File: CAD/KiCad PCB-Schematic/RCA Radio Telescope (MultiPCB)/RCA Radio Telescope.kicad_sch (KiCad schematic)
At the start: 10 parts, among them J1 Screw_Terminal_01x04, J12 3V In For LNA, J2 9-12V From PoE Splitter, J3 3V Out For LNA, J4 5V Out For Filter Board, J6 USB_B_MICRO, U1 ZX60-P33ULN+, U2 ADALM Pluto SDR

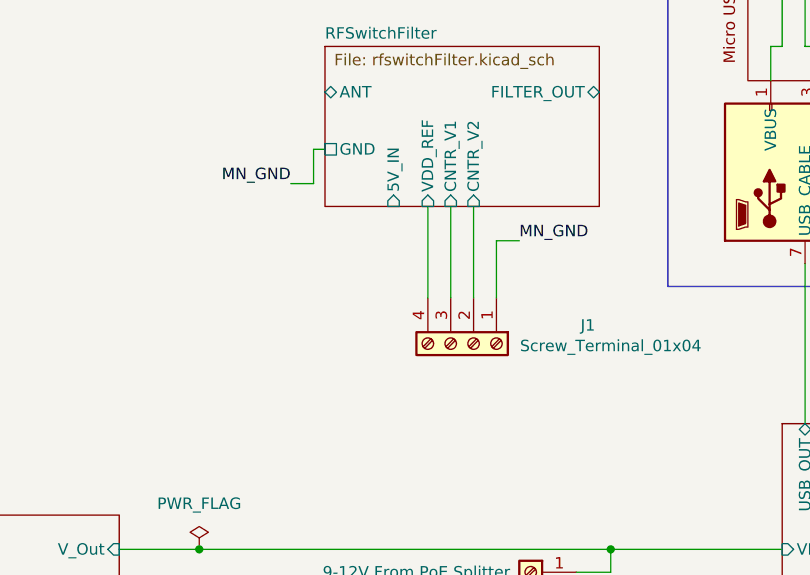
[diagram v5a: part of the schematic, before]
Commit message: Added 4 RF Board Designs into KiCAD project
- Added Matched SMD Filter Board, Matched Distributive Filter Board, RF Switch Filter Board, and kept original SMD Filter Board
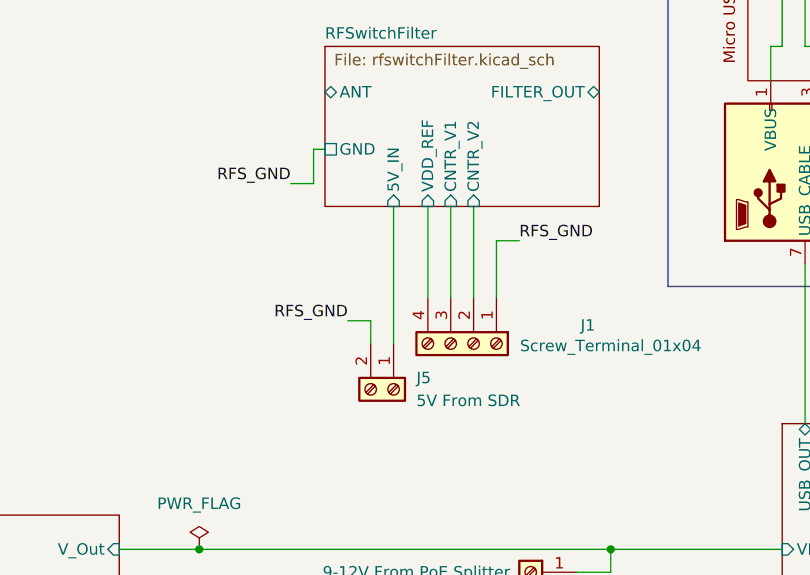
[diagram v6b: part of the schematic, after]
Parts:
- added J5: 5V From SDR, Library:CONN_1729128_PXC, symbol Connector:Screw_Terminal_01x02
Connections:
- net RFSwitchFilter/5V_IN: now also J5.1 (Pin_1)
- net MN_GND renamed RFS_GND
- net RFS_GND: now also J5.2 (Pin_2)
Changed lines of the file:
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@@
 	(title_block
 		(title "RCA Radio Telescope System")
-		(date "2025-04-03")
-		(rev "Version 2.0")
+		(date "2025-04-29")
+		(rev "Version 2.1")
 	)
 	(junction
@@
 	(wire
 		(pts
+			(xy 127 93.98) (xy 127 96.52)
+		)
+		(stroke
+			(width 0)
+			(type default)
+		)
+	)
+	(wire
+		(pts
 			(xy 181.61 63.5) (xy 181.61 67.31)
 		)
@@
 	(wire
 		(pts
+			(xy 129.54 81.28) (xy 129.54 96.52)
+		)
+		(stroke
+			(width 0)
+			(type default)
+		)
+	)
+	(wire
+		(pts
 			(xy 182.88 63.5) (xy 187.96 63.5)
 		)
@@
 		(pts
 			(xy 179.07 63.5) (xy 179.07 67.31)
+		)
+		(stroke
+			(width 0)
+			(type default)
+		)
+	)
+	(wire
+		(pts
+			(xy 124.46 93.98) (xy 127 93.98)
 		)
 		(stroke
@@
 	(label "SDR_GPO_0"
 		(at 209.55 36.83 0)
+		(fields_autoplaced yes)
 		(effects
 			(font
@@
 	(label "POWERDATA_GND"
 		(at 229.87 137.16 180)
+		(fields_autoplaced yes)
 		(effects
 			(font
@@
 		)
 	)
-	(label "SDR_GPO_GND"
-		(at 209.55 46.99 0)
+	(label "RFS_GND"
+		(at 124.46 93.98 180)
+		(fields_autoplaced yes)
 		(effects
 			(font
 				(size 1.27 1.27)
 			)
-			(justify left bottom)
-		)
-	)
-	(label "POWERDATA_GND"
-		(at 222.25 123.19 0)
+			(justify right bottom)
+		)
+	)
+	(label "SDR_GPO_GND"
+		(at 209.55 46.99 0)
+		(fields_autoplaced yes)
 		(effects
 			(font
@@
 		)
 	)
-	(label "SDR_GPO_1"
-		(at 209.55 39.37 0)
+	(label "POWERDATA_GND"
+		(at 222.25 123.19 0)
+		(fields_autoplaced yes)
 		(effects
 			(font
@@
 		)
 	)
-	(label "SDR_GPO_VDD"
-		(at 209.55 34.29 0)
+	(label "SDR_GPO_1"
+		(at 209.55 39.37 0)
+		(fields_autoplaced yes)
 		(effects
 			(font
@@
 		)
 	)
-	(label "POWERDATA_GND"
-		(at 229.87 113.03 180)
+	(label "SDR_GPO_VDD"
+		(at 209.55 34.29 0)
+		(fields_autoplaced yes)
 		(effects
 			(font
 				(size 1.27 1.27)
 			)
-			(justify right bottom)
+			(justify left bottom)
 		)
 	)
 	(label "POWERDATA_GND"
-		(at 156.21 124.46 0)
+		(at 229.87 113.03 180)
+		(fields_autoplaced yes)
 		(effects
 			(font
 				(size 1.27 1.27)
 			)
-			(justify left bottom)
-		)
-	)
-	(label "MN_GND"
-		(at 143.51 85.09 0)
+			(justify right bottom)
+		)
+	)
+	(label "POWERDATA_GND"
+		(at 156.21 124.46 0)
+		(fields_autoplaced yes)
 		(effects
 			(font
@@
 		)
 	)
-	(label "MN_GND"
+	(label "RFS_GND"
+		(at 143.51 85.09 0)
+		(fields_autoplaced yes)
+		(effects
+			(font
+				(size 1.27 1.27)
+			)
+			(justify left bottom)
+		)
+	)
+	(label "RFS_GND"
 		(at 118.11 78.74 180)
+		(fields_autoplaced yes)
 		(effects
 			(font
@@
 					(unit 1)
 				)
+			)
+		)
+	)
+	(symbol
+		(lib_id "Connector:Screw_Terminal_01x02")
+		(at 129.54 101.6 270)
+		(unit 1)
+		(exclude_from_sim no)
+		(in_bom yes)
+		(on_board yes)
+		(dnp no)
+		(fields_autoplaced yes)
+		(property "Reference" "J5"
+			(at 132.08 100.3299 90)
+			(effects
+				(font
+					(size 1.27 1.27)
+				)
+				(justify left)
+			)
+		)
+		(property "Value" "5V From SDR"
+			(at 132.08 102.8699 90)
+			(effects
+				(font
+					(size 1.27 1.27)
+				)
+				(justify left)
+			)
+		)
+		(property "Footprint" "Library:CONN_1729128_PXC"
+			(at 129.54 101.6 0)
+			(effects
+				(font
+					(size 1.27 1.27)
+				)
+				(hide yes)
+			)
+		)
+		(property "Datasheet" "~"
+			(at 129.54 101.6 0)
+			(effects
+				(font
+					(size 1.27 1.27)
+				)
+				(hide yes)
+			)
+		)
+		(property "Description" "Generic screw terminal, single row, 01x02, script generated (kicad-library-utils/schlib/autogen/connector/)"
+			(at 129.54 101.6 0)
+			(effects
+				(font
+					(size 1.27 1.27)
+				)
+				(hide yes)
+			)
+		)
+		(pin "2"
+		)
+		(pin "1"
+		)
+		(instances
+			(project "RCA Radio Telescope"
+				(path "/1630c5ee-b70a-455e-85ba-86a73955b8fd"
+					(reference "J5")
+					(unit 1)
+				)

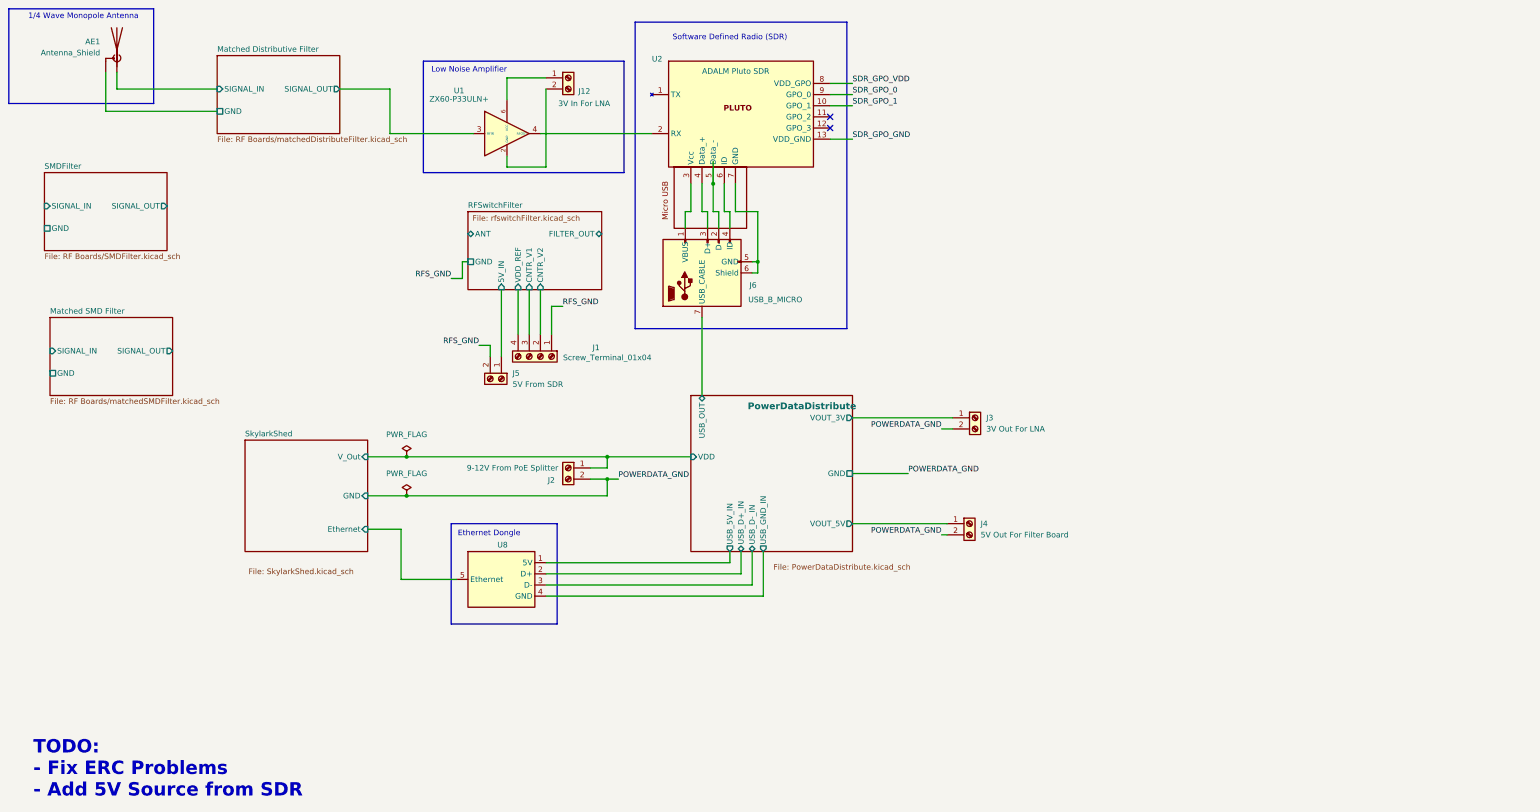
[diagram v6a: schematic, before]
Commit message: Updated Schematic to Fix USB/PMOS issues and Minor Fixes
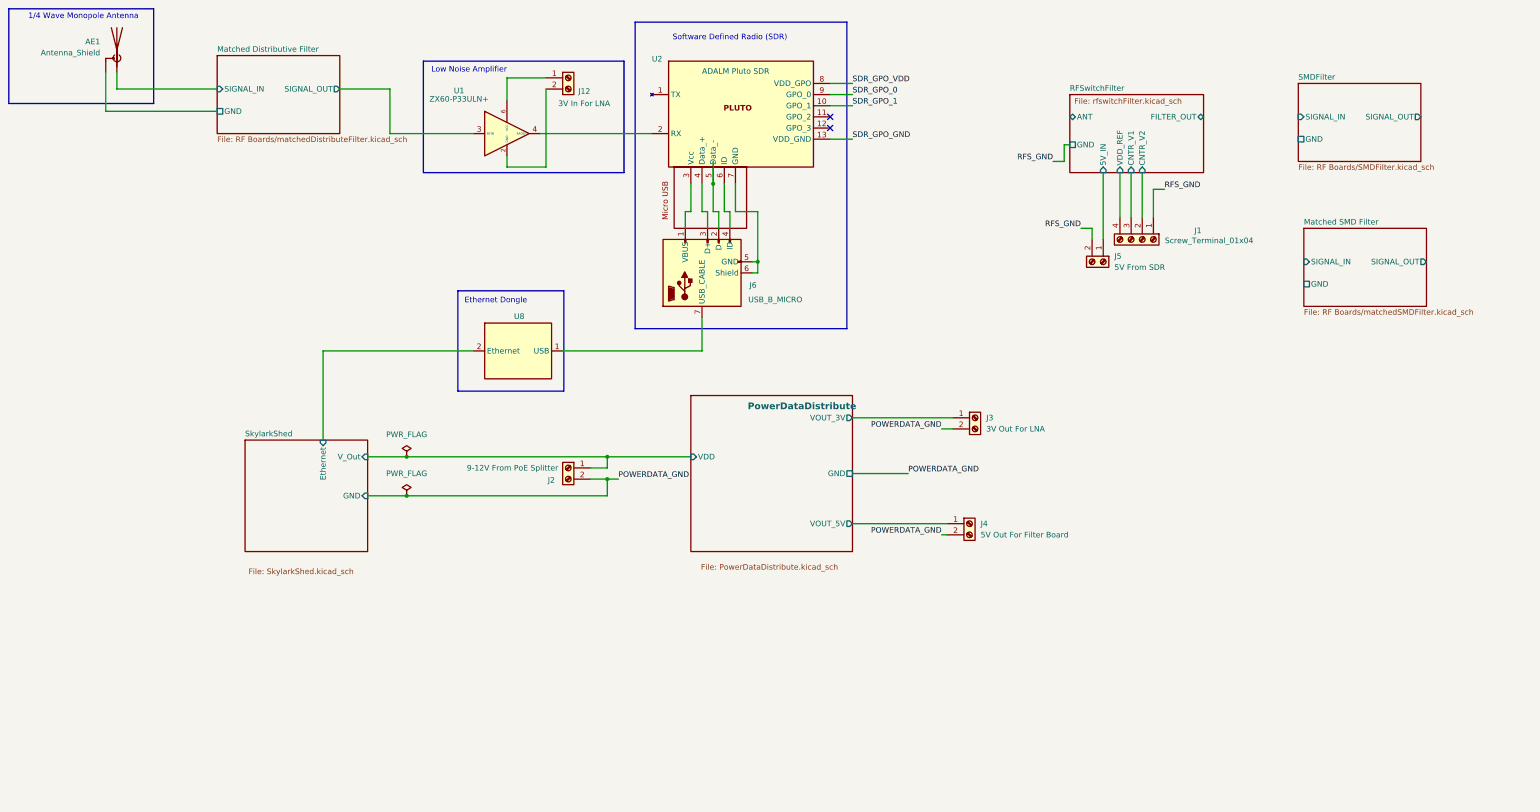
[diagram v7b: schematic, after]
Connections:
- net PowerDataDistribute/USB_D+_IN is gone; now on net SkylarkShed/Ethernet: U8.2 (Ethernet)
- net PowerDataDistribute/USB_OUT is gone; now on an unnamed net: J6.7 (USB_CABLE)
- net SkylarkShed/Ethernet: no longer U8.5 (Ethernet)
- net PowerDataDistribute/USB_5V_IN: no longer names the net of U8.1 (USB)
- removed net PowerDataDistribute/USB_D-_IN: U8.3 (D-)
- removed net PowerDataDistribute/USB_GND_IN: U8.4 (GND)
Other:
- sheet PowerDataDistribute ports: added none; removed USB_5V_IN, USB_D+_IN, USB_D-_IN, USB_GND_IN, USB_OUT
- note removed: "TODO: - Fix ERC Problems - Add 5V Source from SDR"
- moved on the sheet: J1, J5
